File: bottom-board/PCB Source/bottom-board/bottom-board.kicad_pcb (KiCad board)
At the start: 4 copper layers, 193 x 93 mm, 307 parts, among them J1 AS0A823-H4SB-7H, P1 USB_B, P10 JACK_TRS_6PINS, P11 JACK_TRS_6PINS, P12 JACK_TRS_6PINS, P13 RJ45, P14 AudioJack3, P2 USB_A, P3 BARREL_JACK, P5 HMI_DATA, P6 AudioJack3, P7 AudioJack3, P8 SERIAL_DEBUG, P9 JACK_TRS_6PINS, Q1 2N7002, Q10 MMBFJ111, Q12 2N7002, Q13 2N7002, Q2 2N7002, Q3 MMBFJ111, Q4 MMBFJ111, Q5 MMBFJ111, Q6 MMBFJ111, Q7 2N7002, Q8 2N7002, Q9 MMBFJ111, U1 TS2596, U10 RT9742MNGJ5, U11 6N137S, U12 ISL83491, U13 AP2120N-3.3, U2 TL750M10CKVURG3, U3 CS4265, U4 AT24CS08-STUM, U5 LM4562, U6 OPA1678, U7 OPA1678, U8 LM4811, U9 LD1117S50TR_SOT223, X1 24.576MHz

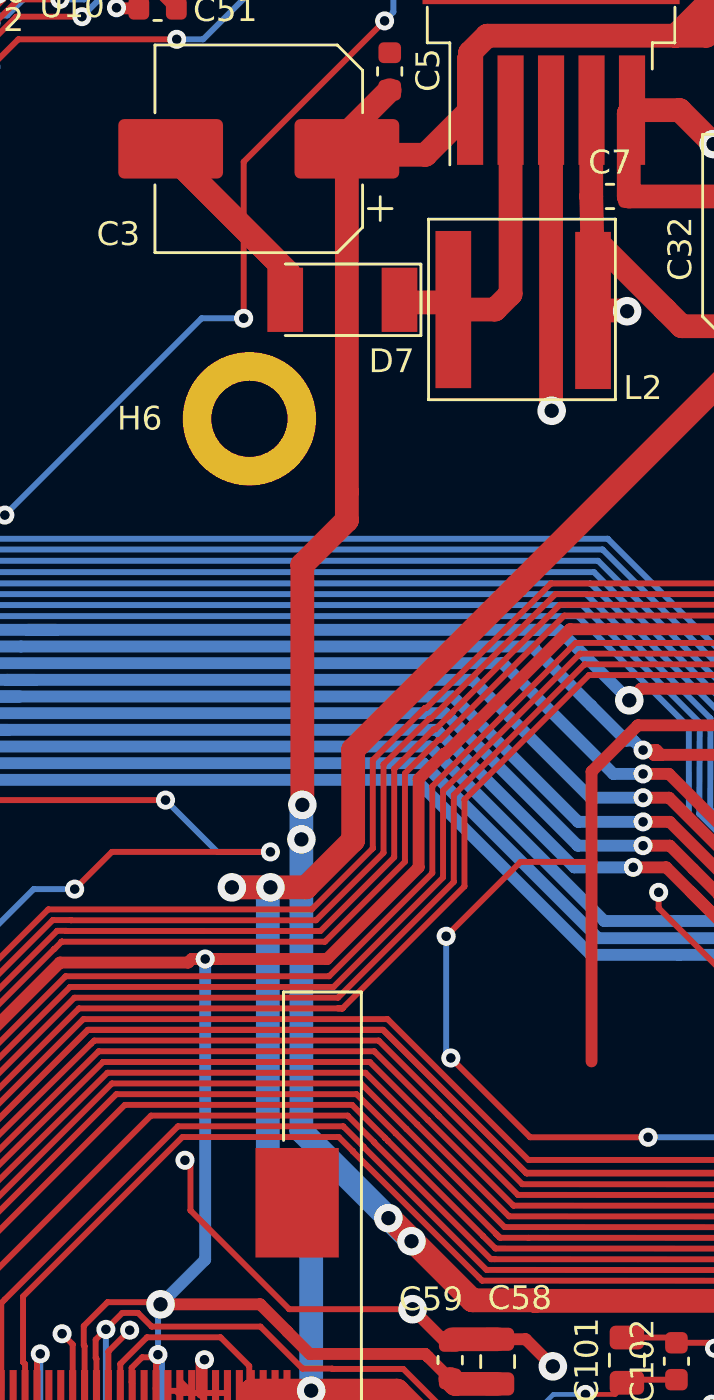
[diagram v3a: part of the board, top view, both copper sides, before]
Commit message: supply topboard with 5V instead of 12
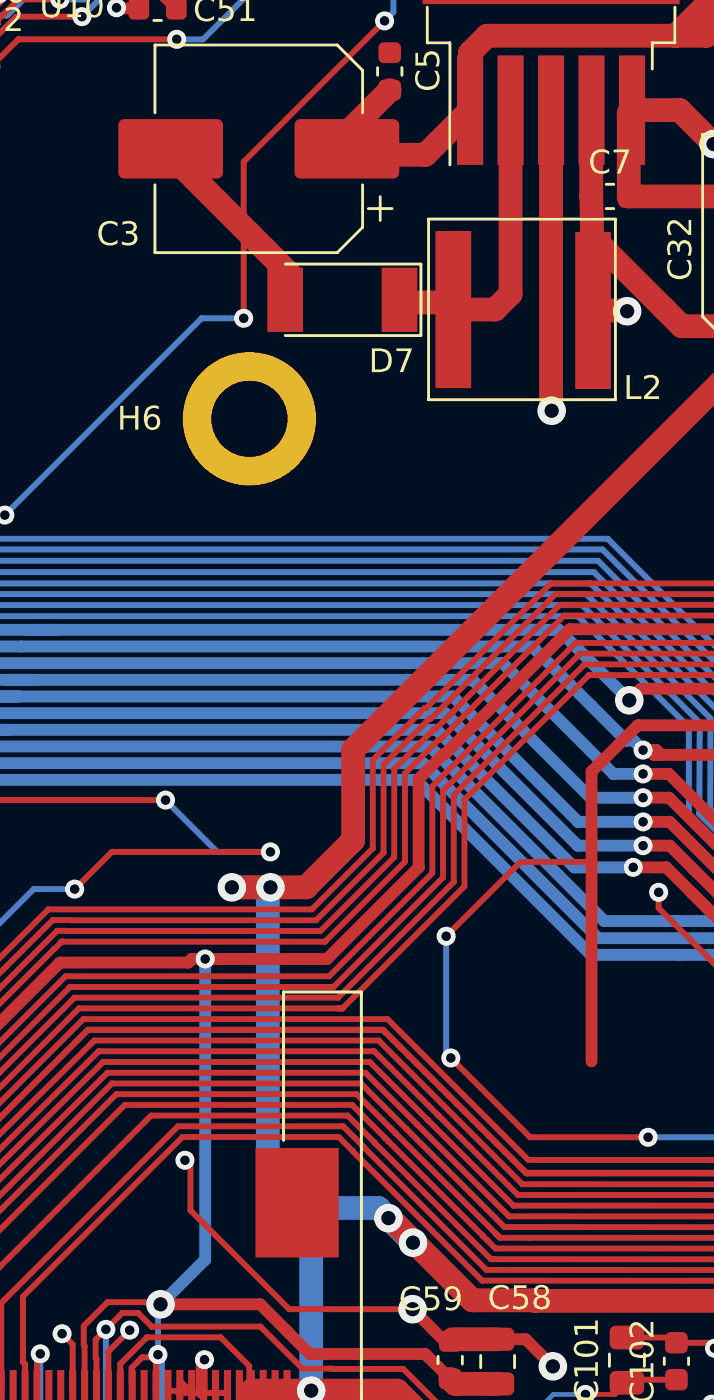
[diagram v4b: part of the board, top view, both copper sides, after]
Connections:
- P5 pad 3: +12V -> +5V
- P5 pad 5: +12V -> +5V
- P5 pad 7: +12V -> +5V
- P5 pad 9: +12V -> +5V
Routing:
- net +12V: track 174.2 -> 64.6 mm, vias 4 -> 0
- net +5V: track 151.8 -> 217.9 mm, vias 10 -> 12
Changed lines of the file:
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@@
     (thickness 1.6)
     (drawings 354)
-    (tracks 4384)
+    (tracks 4376)
     (zones 0)
     (modules 307)
@@
   )
   (setup
-    (last_trace_width 0.25)
+    (last_trace_width 1)
     (user_trace_width 0.2)
     (user_trace_width 0.45)
@@
       (net 174 "Net-(P5-Pad10)"))
     (pad 9 thru_hole oval (at 0 10.16 90) (size 1.7272 1.7272) (drill 1.016) (layers *.Cu *.Mask F.SilkS)
-      (net 2 +12V))
+      (net 3 +5V))
     (pad 8 thru_hole oval (at 2.54 7.62 90) (size 1.7272 1.7272) (drill 1.016) (layers *.Cu *.Mask F.SilkS)
       (net 173 "Net-(P5-Pad8)"))
     (pad 7 thru_hole oval (at 0 7.62 90) (size 1.7272 1.7272) (drill 1.016) (layers *.Cu *.Mask F.SilkS)
-      (net 2 +12V))
+      (net 3 +5V))
     (pad 6 thru_hole oval (at 2.54 5.08 90) (size 1.7272 1.7272) (drill 1.016) (layers *.Cu *.Mask F.SilkS)
       (net 117 HMI_RFU_RX))
     (pad 5 thru_hole oval (at 0 5.08 90) (size 1.7272 1.7272) (drill 1.016) (layers *.Cu *.Mask F.SilkS)
-      (net 2 +12V))
+      (net 3 +5V))
     (pad 4 thru_hole oval (at 2.54 2.54 90) (size 1.7272 1.7272) (drill 1.016) (layers *.Cu *.Mask F.SilkS)
       (net 116 HMI_RFU_TX))
     (pad 3 thru_hole oval (at 0 2.54 90) (size 1.7272 1.7272) (drill 1.016) (layers *.Cu *.Mask F.SilkS)
-      (net 2 +12V))
+      (net 3 +5V))
     (pad 2 thru_hole oval (at 2.54 0 90) (size 1.7272 1.7272) (drill 1.016) (layers *.Cu *.Mask F.SilkS)
       (net 65 GNDD))
@@
   (module Uno:SRN8040TA (layer F.Cu)
     (at 148.25 78.75 270)
+    (attr smd)
     (fp_text reference L2 (at 3.292 -2.88) (layer F.SilkS)
       (effects (font (size 1 1) (thickness 0.15)))
@@
     (descr "fiducial in-circuit")
     (tags "fiducial in-circuit")
+    (attr smd)
     (fp_text reference FID1 (at 0 2.3) (layer F.SilkS)
       (effects (font (size 1 1) (thickness 0.15)))
@@
     (descr "fiducial in-circuit")
     (tags "fiducial in-circuit")
+    (attr smd)
     (fp_text reference FID2 (at 0 2.3) (layer F.SilkS)
       (effects (font (size 1 1) (thickness 0.15)))
@@
     (descr "fiducial in-circuit")
     (tags "fiducial in-circuit")
+    (attr smd)
     (fp_text reference FID3 (at 0 2.3) (layer F.SilkS)
       (effects (font (size 1 1) (thickness 0.15)))
@@
   (module Uno:6N137S (layer F.Cu)
     (at 198.72 63.34 270)
+    (attr smd)
     (fp_text reference U11 (at -5.5118 0 270) (layer F.SilkS)
       (effects (font (size 0.48 0.48) (thickness 0.015)))
@@
       (effects (font (size 1 1) (thickness 0.15)))
     )
-    (fp_text user %R (at 0 0) (layer F.Fab)
-      (effects (font (size 0.4 0.4) (thickness 0.06)))
-    )
     (fp_line (start -0.8 0.4125) (end -0.8 -0.4125) (layer F.Fab) (width 0.1))
     (fp_line (start -0.8 -0.4125) (end 0.8 -0.4125) (layer F.Fab) (width 0.1))
@@
     (fp_line (start 1.48 -0.73) (end 1.48 0.73) (layer F.CrtYd) (width 0.05))
     (fp_line (start 1.48 0.73) (end -1.48 0.73) (layer F.CrtYd) (width 0.05))
+    (fp_text user %R (at 0 0) (layer F.Fab)
+      (effects (font (size 0.4 0.4) (thickness 0.06)))
+    )
     (pad 2 smd roundrect (at 0.825 0 180) (size 0.8 0.95) (layers F.Cu F.Paste F.Mask) (roundrect_rratio 0.25)
       (net 4 +5VA))
@@
   (segment (start 163.460002 63) (end 166.175 60.285002) (width 1) (layer F.Cu) (net 2))
   (segment (start 166.175 60.285002) (end 166.175 57.975) (width 1) (layer F.Cu) (net 2))
-  (segment (start 138.7 72.25) (end 138.7 86.4) (width 1) (layer F.Cu) (net 2))
-  (segment (start 138.7 87.6) (end 138.7 86.4) (width 1) (layer F.Cu) (net 2))
-  (via (at 136.83 99.55) (size 1.2) (drill 0.6) (layers F.Cu B.Cu) (net 2))
-  (segment (start 138.7 87.6) (end 136.83 89.47) (width 1) (layer F.Cu) (net 2))
-  (segment (start 136.83 89.47) (end 136.83 99.55) (width 1) (layer F.Cu) (net 2))
-  (via (at 136.79 101) (size 1.2) (drill 0.6) (layers F.Cu B.Cu) (net 2))
-  (segment (start 136.79 99.59) (end 136.83 99.55) (width 1) (layer B.Cu) (net 2))
-  (segment (start 136.79 101) (end 136.79 99.59) (width 1) (layer B.Cu) (net 2))
-  (segment (start 195.44 125.44) (end 187.82 125.44) (width 1) (layer F.Cu) (net 2))
-  (via (at 140.444516 116.905484) (size 1.2) (drill 0.6) (layers F.Cu B.Cu) (net 2))
-  (segment (start 136.79 113.250968) (end 140.444516 116.905484) (width 1) (layer B.Cu) (net 2))
-  (segment (start 136.79 101) (end 136.79 113.250968) (width 1) (layer B.Cu) (net 2))
-  (via (at 141.414516 117.875484) (size 1.2) (drill 0.6) (layers F.Cu B.Cu) (net 2))
-  (segment (start 140.444516 116.905484) (end 141.414516 117.875484) (width 1) (layer B.Cu) (net 2))
+  (segment (start 195.44 125.44) (end 187.82 125.44) (width 1) (layer F.Cu) (net 3))
   (segment (start 160.65293 63) (end 163.460002 63) (width 1) (layer F.Cu) (net 2))
-  (segment (start 186.571314 127.91) (end 187.82 126.661314) (width 1) (layer F.Cu) (net 2))
-  (segment (start 162.49 127.91) (end 186.571314 127.91) (width 1) (layer F.Cu) (net 2))
-  (segment (start 154.96 120.38) (end 162.49 127.91) (width 1) (layer F.Cu) (net 2))
-  (segment (start 146.576778 120.356777) (end 146.600001 120.38) (width 1) (layer F.Cu) (net 2))
-  (segment (start 187.82 126.661314) (end 187.82 125.44) (width 1) (layer F.Cu) (net 2))
-  (segment (start 143.966777 120.356777) (end 146.576778 120.356777) (width 1) (layer F.Cu) (net 2))
-  (segment (start 146.600001 120.38) (end 154.96 120.38) (width 1) (layer F.Cu) (net 2))
-  (segment (start 140.48 116.87) (end 143.966777 120.356777) (width 1) (layer F.Cu) (net 2))
+  (segment (start 186.571314 127.91) (end 187.82 126.661314) (width 1) (layer F.Cu) (net 3))
+  (segment (start 162.49 127.91) (end 186.571314 127.91) (width 1) (layer F.Cu) (net 3))
+  (segment (start 154.96 120.38) (end 162.49 127.91) (width 1) (layer F.Cu) (net 3))
+  (segment (start 146.576778 120.356777) (end 146.600001 120.38) (width 1) (layer F.Cu) (net 3))
+  (segment (start 187.82 126.661314) (end 187.82 125.44) (width 1) (layer F.Cu) (net 3))
+  (segment (start 143.966777 120.356777) (end 146.576778 120.356777) (width 1) (layer F.Cu) (net 3))
+  (segment (start 146.600001 120.38) (end 154.96 120.38) (width 1) (layer F.Cu) (net 3))
+  (segment (start 140.48 116.87) (end 143.966777 120.356777) (width 1) (layer F.Cu) (net 3))
   (segment (start 169.759999 50.719999) (end 171.45 52.41) (width 1) (layer F.Cu) (net 2))
   (segment (start 166.880001 50.719999) (end 169.759999 50.719999) (width 1) (layer F.Cu) (net 2))
@@
   (segment (start 129.42198 132.65839) (end 129.410001 132.646411) (width 0.25) (layer F.Cu) (net 3))
   (segment (start 129.42198 133.483022) (end 129.42198 132.65839) (width 0.25) (layer F.Cu) (net 3))
+  (via (at 140.444516 116.905484) (size 1.2) (drill 0.6) (layers F.Cu B.Cu) (net 3))
+  (segment (start 140.019032 116.48) (end 140.444516 116.905484) (width 1) (layer B.Cu) (net 3))
+  (segment (start 137.2 116.48) (end 140.019032 116.48) (width 1) (layer B.Cu) (net 3))
+  (via (at 141.475766 117.936734) (size 1.2) (drill 0.6) (layers F.Cu B.Cu) (net 3))
+  (segment (start 140.444516 116.905484) (end 141.475766 117.936734) (width 1) (layer B.Cu) (net 3))
   (segment (start 167.2 99.8) (end 167.2 97.55) (width 0.5) (layer F.Cu) (net 4))
   (segment (start 166.05 100.95) (end 167.2 99.8) (width 0.5) (layer F.Cu) (net 4))

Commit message: update production files
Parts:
- U10: value RT9742MNGJ5 -> TPS2001DDBVR
- moved U10 0.16 mm to (127.4, 63.2), turned to 180 degrees
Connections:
- P7 pad R: Net-(D12-Pad3) -> Net-(P7-PadR)
- P7 pad T: Net-(P7-PadT) -> Net-(D12-Pad3)
- R49 pad 1: Net-(P7-PadT) -> Net-(P7-PadR)
- U10 pad 3: +5V -> (no net)
- U10 pad 5: Net-(C52-Pad2) -> +5V
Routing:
- net Net-(P7-PadR): track 0.00 -> 19.2 mm
- net GNDD: track 1462.4 -> 1451.8 mm
- net Net-(P7-PadT): track 6.14 -> 0.00 mm
- net USB_HOST_DRV: track 101.9 -> 97.2 mm
- net Net-(D12-Pad3): track 17.2 -> 15.0 mm
- net +5V: track 217.9 -> 219.9 mm

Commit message: minor cleanup
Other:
- board text added: "MOD Devices GmbH http://moddevices.com [MDW-ELE-001] MOD Dwarf - Main Board Rev.: MDW-PX30-V1.00 Date: 2020.12.23"
- board text removed: "MOD Devices GmbH http://moddevices.com [MDW-ELE-001] MOD Dwarf - Main Board Rev.: MDW-PX30-V0.03 Date: 2020.09.18"
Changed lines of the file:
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@@
   (gr_line (start 70.25768 124.05788) (end 70.10768 124.05788) (layer Dwgs.User) (width 0.2))
   (gr_line (start 135.65768 117.75788) (end 137.80768 117.75788) (layer Dwgs.User) (width 0.2))
-  (gr_text "MOD Devices GmbH\nhttp://moddevices.com\n\n[MDW-ELE-001]\nMOD Dwarf - Main Board \nRev.: MDW-PX30-V0.03\nDate: 2020.09.18" (at 244.76 117.31) (layer B.SilkS)
+  (gr_text "MOD Devices GmbH\nhttp://moddevices.com\n\n[MDW-ELE-001]\nMOD Dwarf - Main Board \nRev.: MDW-PX30-V1.00\nDate: 2020.12.23" (at 244.76 117.31) (layer B.SilkS)
     (effects (font (size 1.5 1.5) (thickness 0.3)) (justify left mirror))
   )

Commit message: cleanup BOM lines
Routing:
- net GNDA: track 3563.6 -> 3561.3 mm
- net CODEC_I2C_SDA: track 169.7 -> 171.7 mm
